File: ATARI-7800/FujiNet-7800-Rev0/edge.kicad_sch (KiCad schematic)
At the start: 5 parts, among them J1 Atari7800_Cart_Edge_32

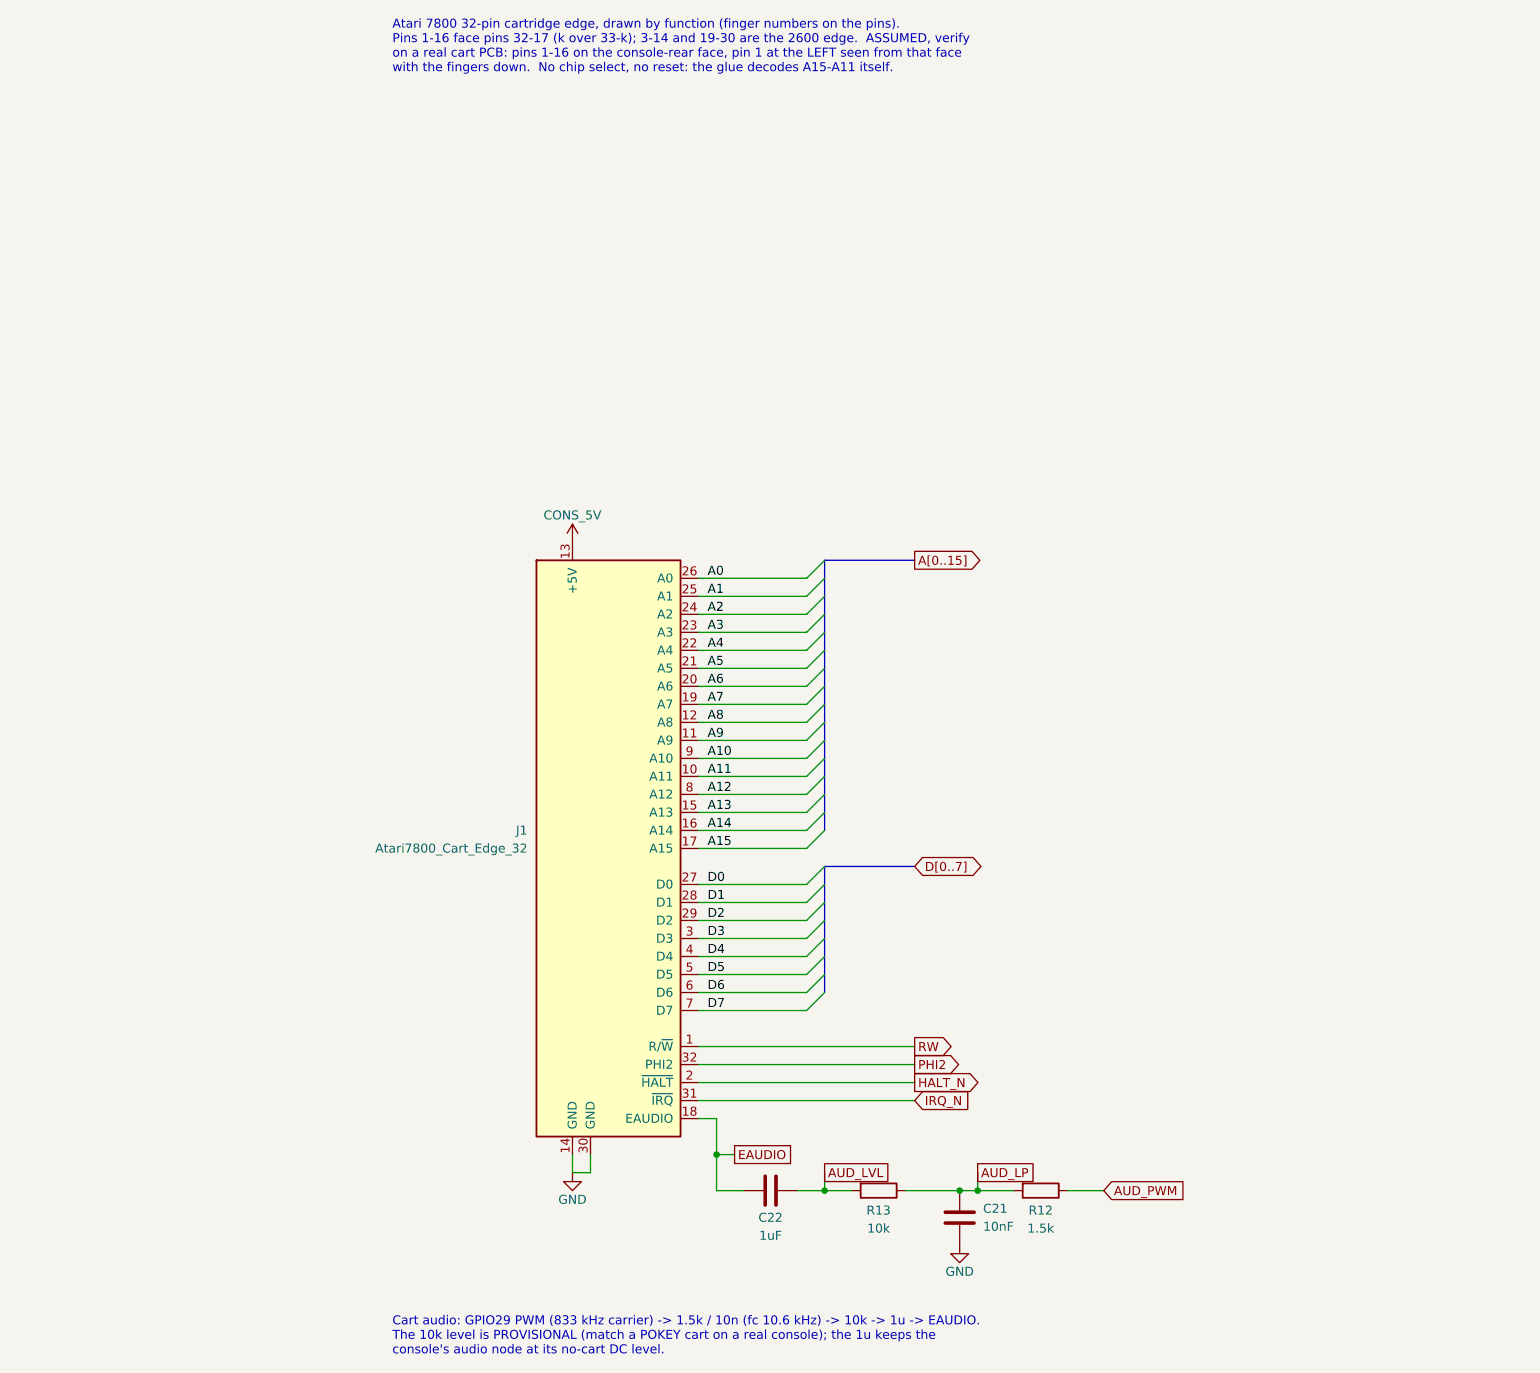
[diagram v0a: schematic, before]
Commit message: ATARI-7800 Rev0: fix the edge, audit the circuit, redraw from the slot, place the board
Edge (board-killer in the schematic-only footprint): the 7800 edge has 18
positions at 2.54 mm with key slots at 3 and 16 for the console's plastic
keys. Pins 1, 2, 15, 16 (and 32, 31, 18, 17) sat one pitch inward, on the
key positions, with no slots and a 42.6 mm tab. tools/edge_geom.py now holds
the geometry (47.0 mm tab, slots centred on +-16.51, 2.4 x 10 mm);
tools/audit/edge_orientation.py checks it against Otaku-flash, tdididit's
boards, the a78-devcart gerbers and this repo's working FujiPlusCart
prototype gerbers (faces and power fingers).

Circuit (console research: Atari C025231 schematic, GCC1702B MARIA spec):
- 4.7k pull-downs on ROM_EN / RAM_EN / A8MASK (RP2350-E9)
- 1k at the /HALT finger (MARIA's HALT is a weak MOS output)
- 10 uF at the console 5V finger; bring-up test pads
- TS-1187A buttons and WS2812C-2020-V1 (the TL3342 and WS2812B-2020
  had 5 in stock at JLC); manufacturer fields for PCBWay
No glue change: R/W is pulled up during MARIA DMA, and the console gates
A15/A14/A12 low while its BIOS is mapped, so CARTSEL never fights it.

Schematic: SMS Rev0's hierarchy (wired root block diagram, hierarchical
labels, netlist parity); sheets in flow order from the slot; the glue
redrawn as a left-to-right gate-depth diagram; references renumbered
from the slot. ERC 0, check_nets 383/383, check_glue 4096/4096.

Board (not yet routed): SMS Rev0's 6-layer pipeline ported. A 72.4 x 115 mm
outline: the stock T-bar width on a 47 x 16.5 mm tab, with the key slots
cut in. Placement variant A (RP over the address fingers, SRAM over the
data fingers): unrouted DRC 0 errors, parity 0, check_vias 0. Shell:
case/FujiNet-7800-Shell.scad. README still describes the old board.

Co-Authored-By: Claude Opus 5.5 <noreply@anthropic.com>
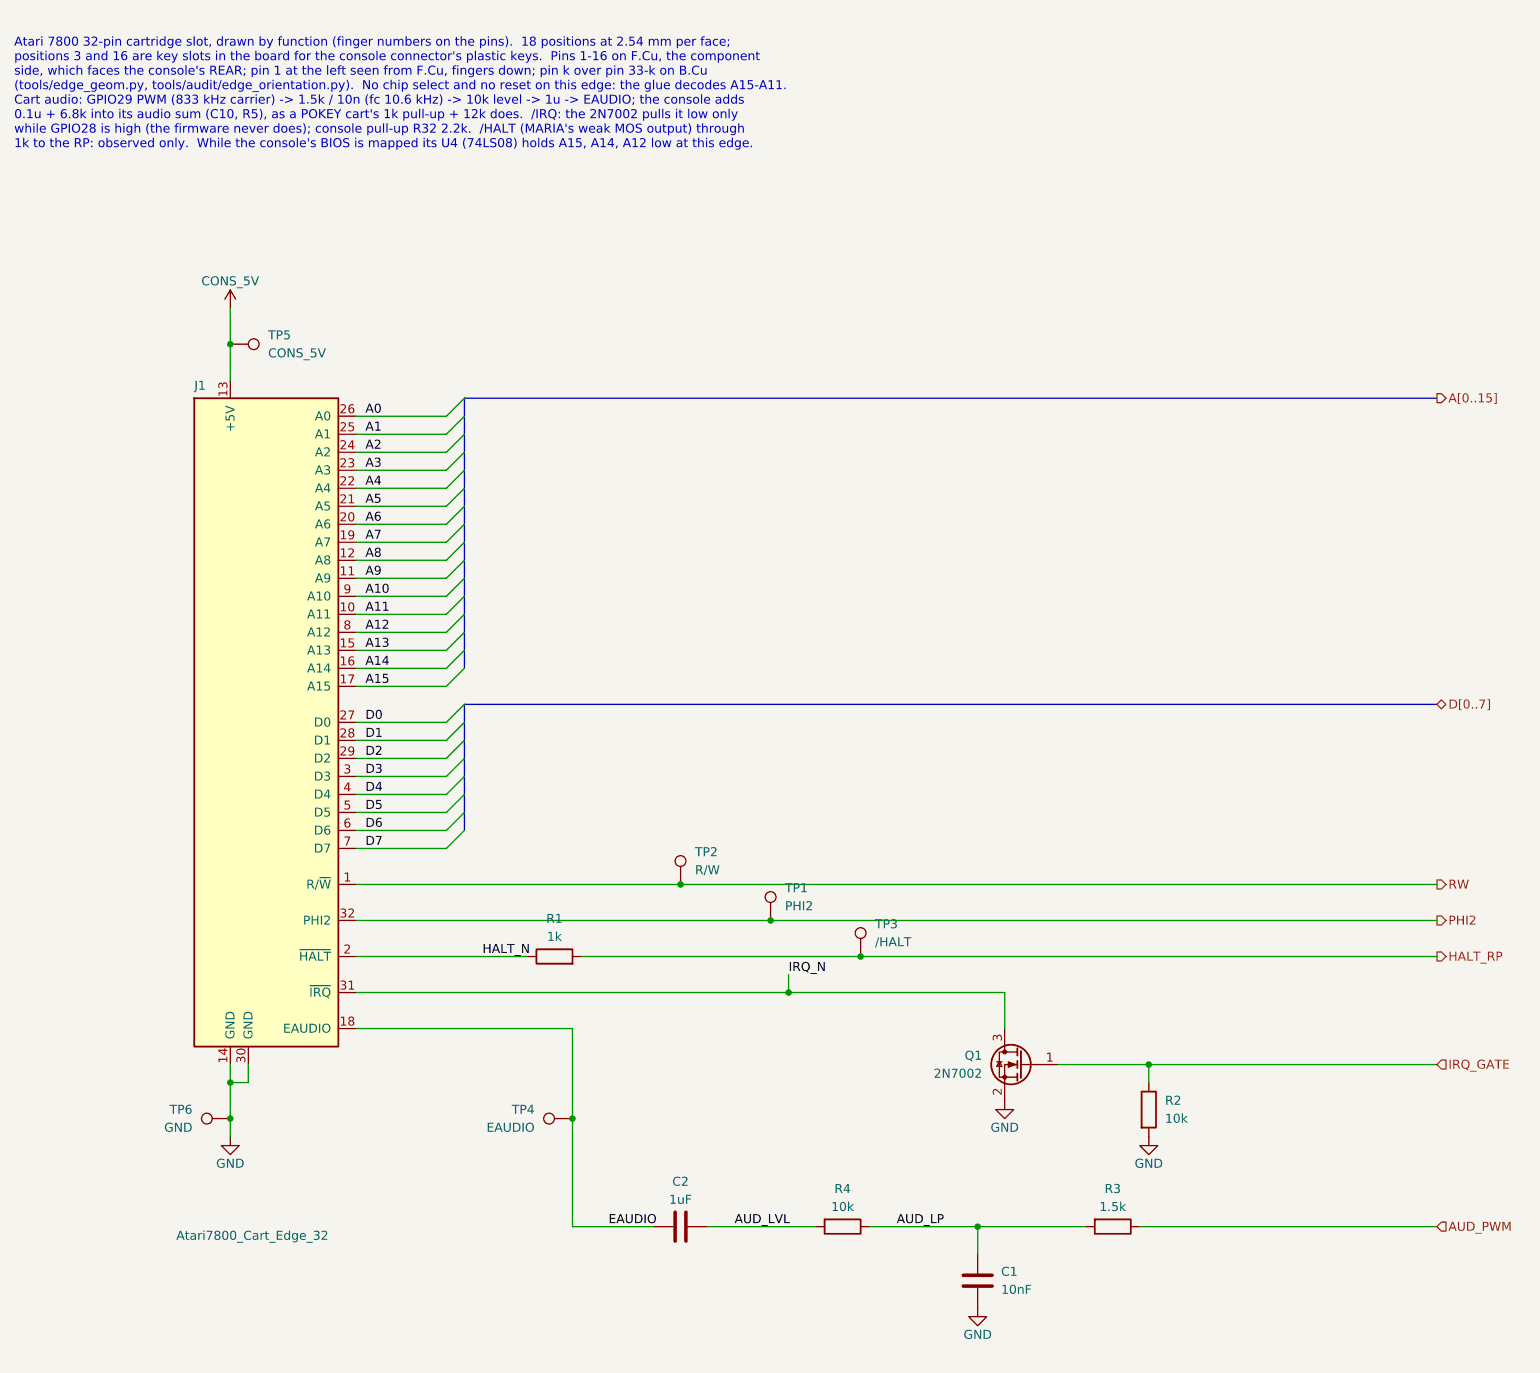
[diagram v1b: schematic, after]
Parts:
- removed C21: 10nF, FujiNet-7800:C_0603_1608Metric, symbol Device:C
- removed C22: 1uF, FujiNet-7800:C_0603_1608Metric, symbol Device:C
- removed R12: 1.5k, FujiNet-7800:R_0603_1608Metric, symbol Device:R
- removed R13: 10k, FujiNet-7800:R_0603_1608Metric, symbol Device:R
- added C1: 10nF, FujiNet-7800:C_0603_1608Metric, symbol Device:C
- added C2: 1uF, FujiNet-7800:C_0603_1608Metric, symbol Device:C
- added Q1: 2N7002, FujiNet-7800:SOT-23, symbol Transistor_FET:2N7002
- added R1: 1k, FujiNet-7800:R_0603_1608Metric, symbol Device:R
- added R2, R4: 10k, FujiNet-7800:R_0603_1608Metric, symbol Device:R
- added R3: 1.5k, FujiNet-7800:R_0603_1608Metric, symbol Device:R
- added TP1: PHI2, FujiNet-7800:TestPoint_Pad_D1.5mm, symbol Connector:TestPoint
- added TP2: R/W, FujiNet-7800:TestPoint_Pad_D1.5mm, symbol Connector:TestPoint
- added TP3: /HALT, FujiNet-7800:TestPoint_Pad_D1.5mm, symbol Connector:TestPoint
- added TP4: EAUDIO, FujiNet-7800:TestPoint_Pad_D1.5mm, symbol Connector:TestPoint
- added TP5: CONS_5V, FujiNet-7800:TestPoint_Pad_D1.5mm, symbol Connector:TestPoint
- added TP6: GND, FujiNet-7800:TestPoint_Pad_D1.5mm, symbol Connector:TestPoint
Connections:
- net AUD_LP: now also C1.1, R3.2, R4.1
- net AUD_LVL: now also C2.1, R4.2
- net AUD_PWM: now also R3.1
- net CONS_5V: now also TP5.1
- net EAUDIO: now also C2.2, TP4.1
- net GND: now also C1.2, Q1.2 (S), R2.2, TP6.1
- net HALT_N: now also R1.1
- net IRQ_N: now also Q1.3 (D)
- net PHI2: now also TP1.1
- net RW: now also TP2.1
- new net HALT_RP: R1.2, TP3.1
- new net IRQ_GATE: Q1.1 (G), R2.1
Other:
- note added: "Atari 7800 32-pin cartridge slot, drawn by function (finger numbers on the pins). 18 positions at 2.54 mm per face; positions 3 and 16 are key slots in the board for the console connector's plastic keys. Pins 1-16 on F.Cu, the component side, which faces the console's REAR; pin 1 at the left seen from F.Cu, fingers down; pin k over pin 33-k on B.Cu (tools/edge_geom.py, tools/audit/edge_orientatio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"
- note removed: "Atari 7800 32-pin cartridge edge, drawn by function (finger numbers on the pins). Pins 1-16 face pins 32-17 (k over 33-k); 3-14 and 19-30 are the 2600 edge. ASSUMED, verify on a real cart PCB: pins 1-16 on the console-rear face, pin 1 at the LEFT seen from that face with the fingers down. No chip select, no reset: the glue decodes A15-A11 itself."
- note removed: "Cart audio: GPIO29 PWM (833 kHz carrier) -> 1.5k / 10n (fc 10.6 kHz) -> 10k -> 1u -> EAUDIO. The 10k level is PROVISIONAL (match a POKEY cart on a real console); the 1u keeps the console's audio node at its no-cart DC level."
- title: FujiNet 7800 Rev0 - 32-pin 7800 cart edge, cart audio -> FujiNet 7800 Rev0 - Cartridge slot, /IRQ, cart audio
- moved on the sheet: J1

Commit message: ATARI-7800 Rev0: route the board, JLCPCB + PCBWay packages, layout review
- Routed 6-layer board: 117 nets; DRC 0/0/0 at every severity with schematic
  parity; check_vias clean. The D0-D7 100R packs now face the RP (rotation
  180, RN1 at x 85.5): with them the other way round, every route left
  RP_D5 open. route_board.sh defaults to the settings that routed it
  (12 Freerouting passes, hybrid strategy).
- Fab packages from one gerber set: exports/jlcpcb (BOM, CPL with measured
  rotations) and exports/pcbway (MPN BOM, centroid, assembly drawing).
- tools/audit/check_gerbers.py checks the fab zips against edge_geom.py:
  slots, both finger faces, mask windows, nothing in the tab. It runs in
  build_all.sh and run_pcb_audit.sh.
- Design review Part 2: routing, the variant runs, and the triage of every
  layout finding. README rewritten for the board, ordering and bring-up.
- R_HALT 10k on the board (sync_pcb_sheets now syncs value, MPN, LCSC and
  description). The audio level resistor is no longer marked provisional.
- Fixes:
  - check_vias tests round pads as circles;
  - gen_sch writes the right top-level sheet (it was the NES template's);
  - the silkscreen title read "FujiNet SMS Rev0";
  - the TS-1187A buttons get a 3D model (the TL3342's) in the library too;
  - PCBWay BOM lines describe the part, not one instance's function;
  - the unused placement variant B is dropped; the tab depth moves into
    edge_geom.

Co-Authored-By: Claude Opus 5.5 <noreply@anthropic.com>
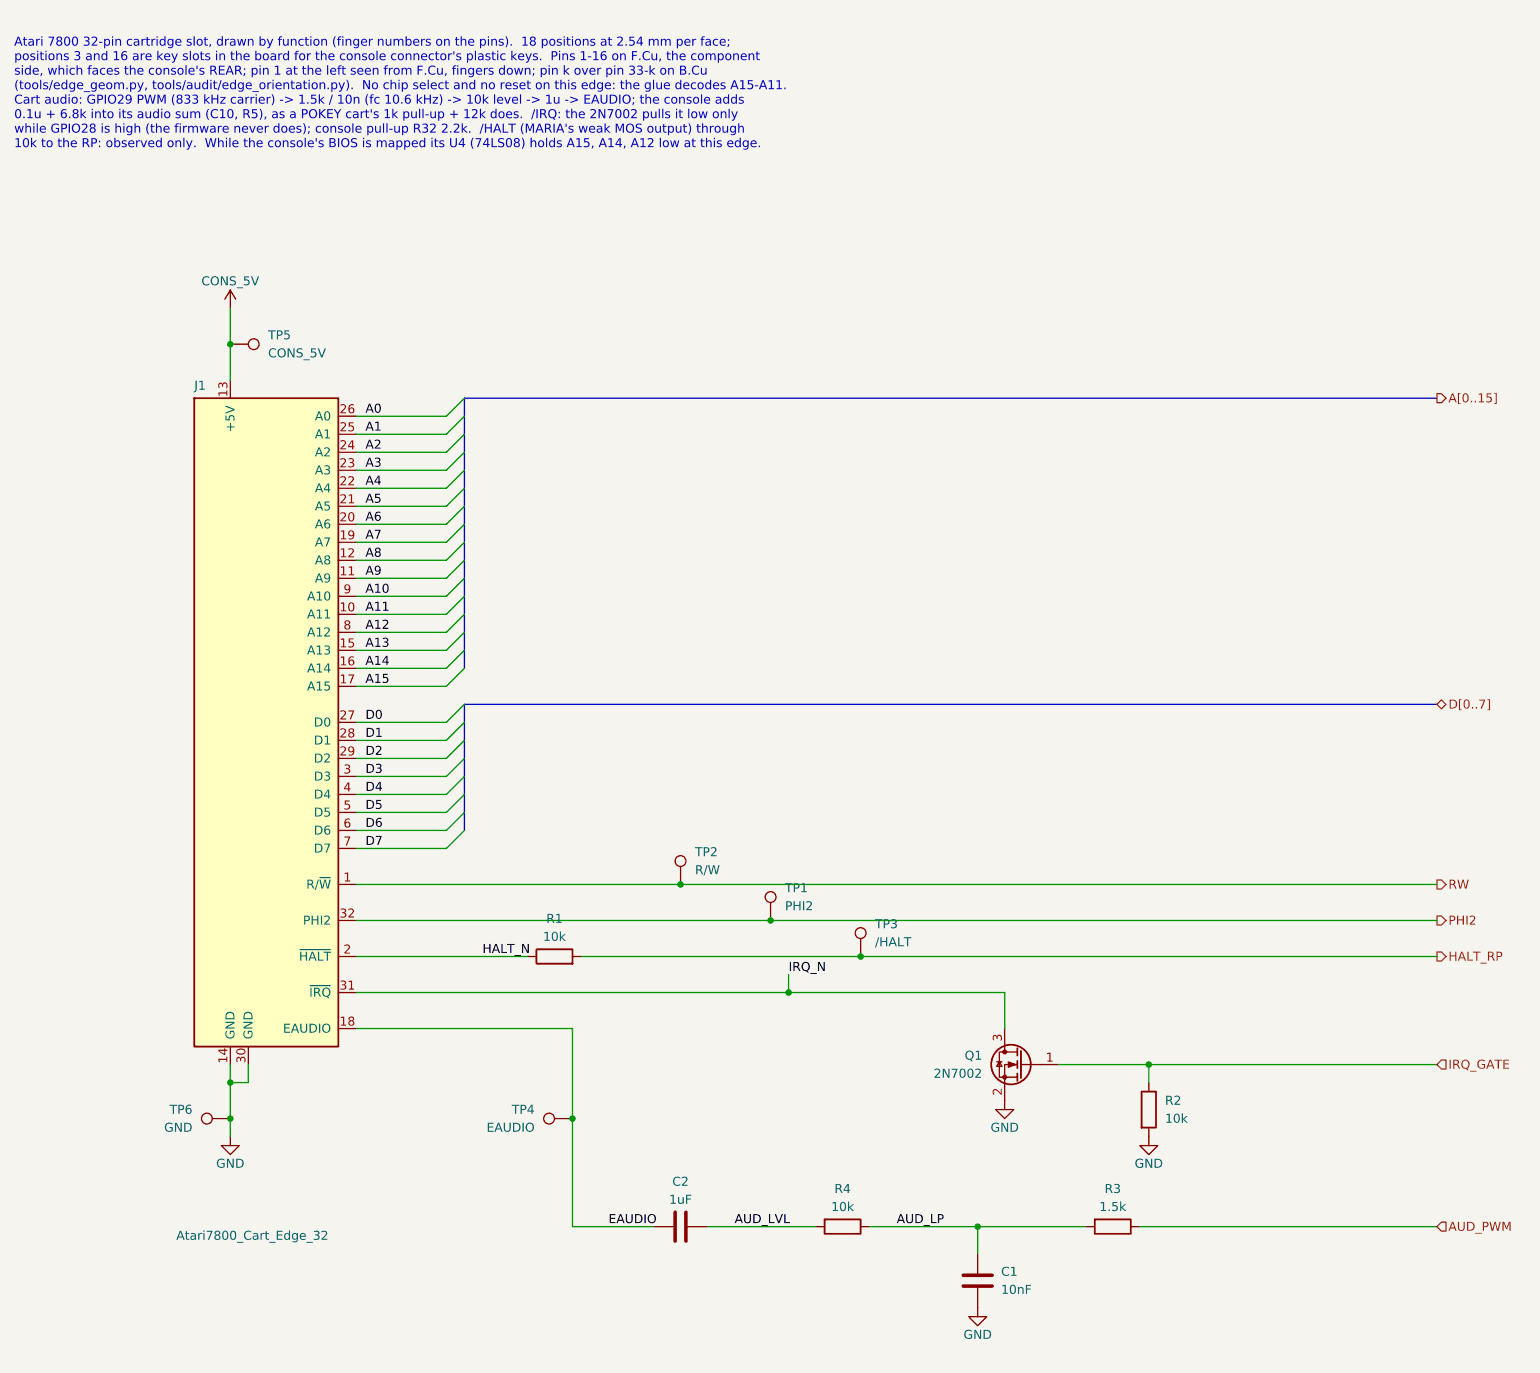
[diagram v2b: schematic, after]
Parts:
- R1: value 1k -> 10k; LCSC C21190 -> C25804; MPN 0603WAF1001T5E -> 0603WAF1002T5E
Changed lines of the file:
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@@
 			)
 		)
-		(property "Value" "1k"
+		(property "Value" "10k"
 			(at 180.34 169.926 90)
 			(effects
@@
 			)
 		)
-		(property "MPN" "0603WAF1001T5E"
+		(property "MPN" "0603WAF1002T5E"
 			(at 180.34 172.72 90)
 			(effects
@@
 			)
 		)
-		(property "LCSC" "C21190"
+		(property "LCSC" "C25804"
 			(at 180.34 172.72 90)
 			(effects
@@
 			)
 		)
-		(property "Description" "bring-up: console /HALT (MARIA DMA), behind its 1k"
+		(property "Description" "bring-up: console /HALT (MARIA DMA), behind its 10k"
 			(at 223.52 172.72 0)
 			(effects
@@
 			)
 		)
-		(property "Description" "EAUDIO level (PROVISIONAL)"
+		(property "Description" "EAUDIO level: a POKEY cart's, +-0.7 dB (spice_checks.py)"
 			(at 220.98 210.82 90)
 			(effects
@@
 		)
 	)
-	(text "Atari 7800 32-pin cartridge slot, drawn by function (finger numbers on the pins).  18 positions at 2.54 mm per face;\npositions 3 and 16 are key slots in the board for the console connector's plastic keys.  Pins 1-16 on F.Cu, the component\nside, which faces the console's REAR; pin 1 at the left seen from F.Cu, fingers down; pin k over pin 33-k on B.Cu\n(tools/edge_geom.py, tools/audit/edge_orientation.py).  No chip select and no reset on this edge: the glue decodes A15-A11.\nCart audio: GPIO29 PWM (833 kHz carrier) -> 1.5k / 10n (fc 10.6 kHz) -> 10k level -> 1u -> EAUDIO; the console adds\n0.1u + 6.8k into its audio sum (C10, R5), as a POKEY cart's 1k pull-up + 12k does.  /IRQ: the 2N7002 pulls it low only\nwhile GPIO28 is high (the firmware never does); console pull-up R32 2.2k.  /HALT (MARIA's weak MOS output) through\n1k to the RP: observed only.  While the console's BIOS is mapped its U4 (74LS08) holds A15, A14, A12 low at this edge."
+	(text "Atari 7800 32-pin cartridge slot, drawn by function (finger numbers on the pins).  18 positions at 2.54 mm per face;\npositions 3 and 16 are key slots in the board for the console connector's plastic keys.  Pins 1-16 on F.Cu, the component\nside, which faces the console's REAR; pin 1 at the left seen from F.Cu, fingers down; pin k over pin 33-k on B.Cu\n(tools/edge_geom.py, tools/audit/edge_orientation.py).  No chip select and no reset on this edge: the glue decodes A15-A11.\nCart audio: GPIO29 PWM (833 kHz carrier) -> 1.5k / 10n (fc 10.6 kHz) -> 10k level -> 1u -> EAUDIO; the console adds\n0.1u + 6.8k into its audio sum (C10, R5), as a POKEY cart's 1k pull-up + 12k does.  /IRQ: the 2N7002 pulls it low only\nwhile GPIO28 is high (the firmware never does); console pull-up R32 2.2k.  /HALT (MARIA's weak MOS output) through\n10k to the RP: observed only.  While the console's BIOS is mapped its U4 (74LS08) holds A15, A14, A12 low at this edge."
 		(exclude_from_sim no)
 		(at 104.14 43.18 0)
